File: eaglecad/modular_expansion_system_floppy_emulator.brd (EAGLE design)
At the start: 90.5 x 100 mm, 35 parts, among them IC1 74LS00N, IC11 74LS20N, IC2 74LS373N, IC3 74LS30N, IC4 74LS244N, IC5 74S74N, IC6 74LS139N, IC7 74LS155N, J1_ADDRESS_CON J1, J1_TEENSY_CON TEENSY_CON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

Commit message: all three boards designed
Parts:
- removed J3_WAIT_AND_INTERRUPT_BLOCK: J3, SparkFun-Connectors:1X20
- added J1-WAIT-AND-INT: WAIT-AND-INT, SparkFun-Connectors:2X4
- moved IC6 20.0 mm to (83.5, 81.0), turned to 270 degrees
- moved H5 0.08 mm to (85.1, 5.08)
- moved H6 0.07 mm to (14.6, 5.08)
- moved H2 0.07 mm to (14.6, 95.2)
- moved H4 0.06 mm to (85.1, 95.2)
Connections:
- removed net INT1*: J3_WAIT_AND_INTERRUPT_BLOCK.2
- removed net INT2*: J3_WAIT_AND_INTERRUPT_BLOCK.3
- removed net INT3*: J3_WAIT_AND_INTERRUPT_BLOCK.4
- removed net INT4*: J3_WAIT_AND_INTERRUPT_BLOCK.5
- removed net INT5*: J3_WAIT_AND_INTERRUPT_BLOCK.6
- removed net INT6*: J3_WAIT_AND_INTERRUPT_BLOCK.7
- removed net INT7*: J3_WAIT_AND_INTERRUPT_BLOCK.8
- removed net WAIT1*: J3_WAIT_AND_INTERRUPT_BLOCK.14
- removed net WAIT2*: J3_WAIT_AND_INTERRUPT_BLOCK.15
- removed net WAIT3*: J3_WAIT_AND_INTERRUPT_BLOCK.16
- removed net WAIT4*: J3_WAIT_AND_INTERRUPT_BLOCK.17
- removed net WAIT5*: J3_WAIT_AND_INTERRUPT_BLOCK.18
- removed net WAIT6*: J3_WAIT_AND_INTERRUPT_BLOCK.19
- removed net WAIT7*: J3_WAIT_AND_INTERRUPT_BLOCK.20
- net INT0*: now also J1-WAIT-AND-INT.1; no longer J3_WAIT_AND_INTERRUPT_BLOCK.1
- net WAIT0*: now also J1-WAIT-AND-INT.2; no longer J3_WAIT_AND_INTERRUPT_BLOCK.13
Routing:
- net INT0*: track 75.1 -> 154.3 mm
- net A11: track 19.4 -> 59.9 mm, vias 1 -> 0
- net XX11X111111XXXX: track 14.2 -> 48.5 mm, vias 0 -> 1
- net 37EX_: track 48.8 -> 80.1 mm, vias 1 -> 0
- net A14: track 15.4 -> 45.8 mm
- net A15: track 15.7 -> 43.9 mm, vias 0 -> 2
- net WAIT0*: track 9.63 -> 30.9 mm, vias 0 -> 1
- net RAS*: track 134.8 -> 119.3 mm
- net 3XXX_: track 9.76 -> 19.2 mm
- net WR*: track 63.5 -> 70.6 mm, vias 2 -> 4
- net RD*: track 28.9 -> 25.2 mm, vias 0 -> 2

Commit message: added text to boards
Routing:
- net D3: track 140.6 -> 144.5 mm
- net D5_HV: track 65.7 -> 68.2 mm
- net P18: track 51.5 -> 52.7 mm
- net 37E4RD_: track 72.2 -> 73.3 mm
- net 37E8WR_: track 35.3 -> 36.2 mm
- net D0_LV: track 48.9 -> 48.0 mm
- net A1_LV: track 66.2 -> 66.9 mm
- net VCC/2: track 151.5 -> 152.2 mm
- net D2_LV: track 51.0 -> 50.4 mm
- net 37E0WR_LV_: track 47.2 -> 46.6 mm
- net 37E4WR_LV_: track 26.6 -> 27.2 mm
- net P17: track 56.3 -> 56.8 mm
- net INTERUPT_TO_TRS80_LV_: track 37.6 -> 38.2 mm
- net A0: track 126.4 -> 125.9 mm
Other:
- board text added: "TRS80MXS Floppy V1.0 Joe Rounceville (C)2019"

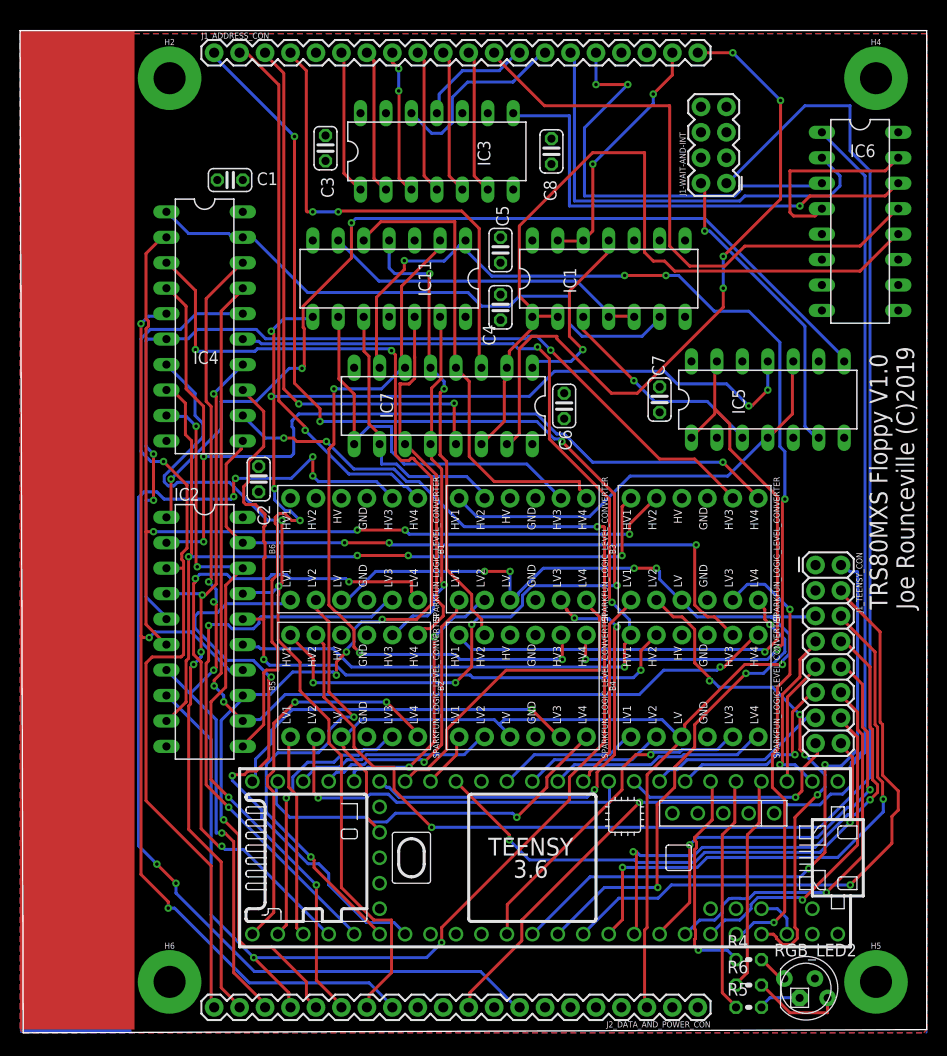
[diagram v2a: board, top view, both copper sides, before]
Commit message: removed soft reset for vdp, added 12 voice sound
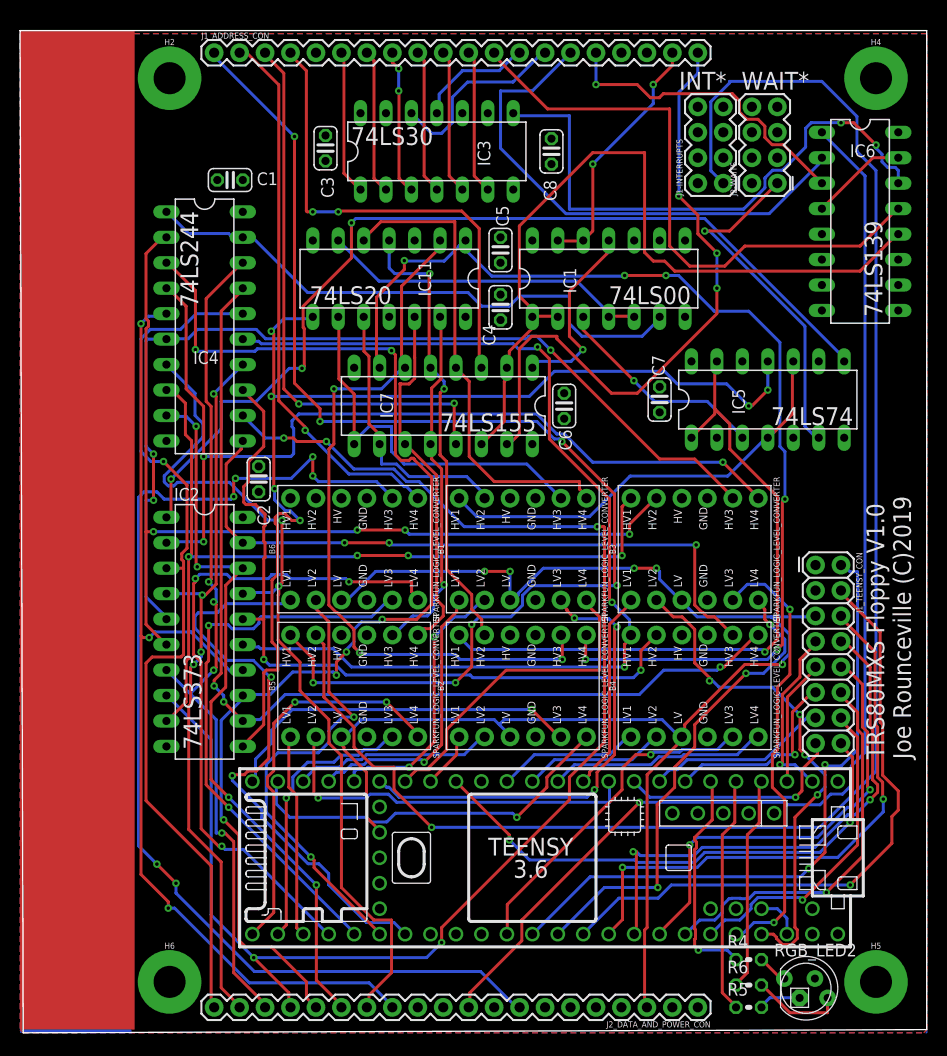
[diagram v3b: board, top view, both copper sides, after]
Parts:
- removed J1-WAIT-AND-INT: WAIT-AND-INT, SparkFun-Connectors:2X4
- added J1-INTERRUPTS: INTERRUPTS, SparkFun-Connectors:2X4
- added J2-WAITS: WAITS, SparkFun-Connectors:2X4
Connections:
- net INT0*: now also J1-INTERRUPTS.1; no longer J1-WAIT-AND-INT.1
- net WAIT0*: now also J2-WAITS.1; no longer J1-WAIT-AND-INT.2
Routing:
- net A15: track 43.9 -> 31.4 mm, vias 2 -> 1
- net 3XXX_: track 19.2 -> 9.72 mm
- net INT0*: track 154.3 -> 163.5 mm
- net XX11X111111XXXX: track 48.5 -> 57.0 mm, vias 1 -> 2
- net WR*: track 70.6 -> 64.6 mm, vias 4 -> 3
- net A14: track 45.8 -> 51.6 mm
- net WAIT0*: track 30.9 -> 35.0 mm
- net RAS*: track 119.3 -> 117.1 mm
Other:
- board text added: "74LS00"
- board text added: "74LS139"
- board text added: "74LS155"
- board text added: "74LS20"
- board text added: "74LS244"
- board text added: "74LS30"
- board text added: "74LS373"
- board text added: "74LS74"
- board text added: "INT*"
- board text added: "WAIT*"

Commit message: boards as they were when sent to allpcb
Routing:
- net D0_LV: track 48.0 -> 51.0 mm
- net VCC/2: track 152.2 -> 153.5 mm
- net D4: track 119.9 -> 120.9 mm
- net D6: track 87.9 -> 87.2 mm
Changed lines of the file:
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@@
 <wire x1="32.25" y1="38.25" x2="33" y2="39" width="0.3" layer="16"/>
 <wire x1="32.25" y1="38" x2="32.25" y2="38.25" width="0.3" layer="16"/>
-<wire x1="31.25" y1="37" x2="32.25" y2="38" width="0.3" layer="1"/>
-<wire x1="31.25" y1="35.6825" x2="31.25" y2="37" width="0.3" layer="1"/>
 <wire x1="30.9325" y1="36" x2="31.25" y2="35.6825" width="0.3" layer="16"/>
 <wire x1="30.9325" y1="36" x2="26.885" y2="36" width="0.3" layer="16"/>
@@
 <wire x1="28.2575" y1="5.08" x2="28.2575" y2="3.4925" width="0.3" layer="1"/>
 <wire x1="28.2575" y1="3.4925" x2="29.21" y2="2.54" width="0.3" layer="1"/>
+<wire x1="31.115" y1="38.1" x2="32.15" y2="38.1" width="0.3" layer="1"/>
+<wire x1="32.15" y1="38.1" x2="32.25" y2="38" width="0.3" layer="1"/>
+<wire x1="31.25" y1="35.6825" x2="30.9524" y2="35.9801" width="0.3" layer="1"/>
+<wire x1="30.9524" y1="37.9374" x2="31.115" y2="38.1" width="0.3" layer="1"/>
+<wire x1="30.9524" y1="35.9801" x2="30.9524" y2="37.9374" width="0.3" layer="1"/>
 </signal>
 <signal name="D6">
@@
 <wire x1="30.5" y1="28.905" x2="30.5" y2="31.25" width="0.3" layer="1"/>
 <wire x1="31.75" y1="27.655" x2="30.5" y2="28.905" width="0.3" layer="1"/>
-<wire x1="31.75" y1="14.5" x2="31.75" y2="27.655" width="0.3" layer="1"/>
-<wire x1="35" y1="11.25" x2="31.75" y2="14.5" width="0.3" layer="1"/>
-<wire x1="36.75" y1="11.25" x2="35" y2="11.25" width="0.3" layer="1"/>
-<wire x1="36.75" y1="6" x2="36.75" y2="11.25" width="0.3" layer="1"/>
+<wire x1="31.75" y1="27.655" x2="31.75" y2="17.8375" width="0.3" layer="1"/>
+<wire x1="36.75" y1="12.8375" x2="36.75" y2="6" width="0.3" layer="1"/>
 <wire x1="34.5" y1="3.75" x2="36.75" y2="6" width="0.3" layer="1"/>
 <wire x1="34.5" y1="2.75" x2="34.5" y2="3.75" width="0.3" layer="1"/>
@@
 <wire x1="14.0694" y1="55.5694" x2="17.9306" y2="59.4306" width="0.3" layer="16"/>
 <wire x1="24.3375" y1="51.1625" x2="20.5725" y2="54.9275" width="0.3" layer="16"/>
+<wire x1="31.75" y1="17.8375" x2="34.521" y2="15.0665" width="0.3" layer="1"/>
+<wire x1="34.521" y1="15.0665" x2="34.521" y2="14.49213125" width="0.3" layer="1"/>
+<wire x1="34.521" y1="14.49213125" x2="35.12963125" y2="13.8835" width="0.3" layer="1"/>
+<wire x1="35.12963125" y1="13.8835" x2="35.704" y2="13.8835" width="0.3" layer="1"/>
+<wire x1="35.704" y1="13.8835" x2="36.75" y2="12.8375" width="0.3" layer="1"/>
 </signal>
 <signal name="D7">
@@
 <contactref element="J1_TEENSY_CON" pad="5"/>
 <wire x1="67.25" y1="41.5" x2="65.75" y2="43" width="0.3" layer="16"/>
-<wire x1="79" y1="41.5" x2="74.6125" y2="41.5" width="0.3" layer="16"/>
-<wire x1="74.6125" y1="41.5" x2="67.25" y2="41.5" width="0.3" layer="16"/>
+<wire x1="79" y1="41.5" x2="74.71251875" y2="41.5" width="0.3" layer="16"/>
+<wire x1="74.71251875" y1="41.5" x2="67.25" y2="41.5" width="0.3" layer="16"/>
 <wire x1="65.75" y1="43" x2="65.7225" y2="43.18" width="0.3" layer="16"/>
 <wire x1="79" y1="41.5" x2="79.0575" y2="41.5925" width="0.3" layer="16"/>
 <wire x1="31.75" y1="43.18" x2="32.315" y2="43.18" width="0.3" layer="16"/>
-<wire x1="65.7225" y1="43.18" x2="65.5" y2="43.25" width="0.3" layer="16"/>
 <wire x1="34.25" y1="21.5" x2="35.5" y2="20.25" width="0.3" layer="1"/>
 <wire x1="34.25" y1="26" x2="34.25" y2="21.5" width="0.3" layer="1"/>
@@
 <wire x1="51.89596875" y1="46.355" x2="49.3673" y2="43.82633125" width="0.3" layer="16"/>
 <via x="60.96" y="46.355" extent="1-16" drill="0.35"/>
-<wire x1="63.5" y1="46.0375" x2="63.1825" y2="46.355" width="0.3" layer="16"/>
-<wire x1="63.5" y1="46.0375" x2="63.5" y2="45.25" width="0.3" layer="16"/>
-<wire x1="65.5" y1="43.25" x2="63.5" y2="45.25" width="0.3" layer="16"/>
-<via x="63.1825" y="46.355" extent="1-16" drill="0.35"/>
-<wire x1="60.96" y1="46.355" x2="63.1825" y2="46.355" width="0.3" layer="1"/>
+<wire x1="65.7225" y1="43.18" x2="65.7225" y2="46.355" width="0.3" layer="16"/>
+<via x="65.7225" y="46.355" extent="1-16" drill="0.35"/>
+<wire x1="60.96" y1="46.355" x2="65.7225" y2="46.355" width="0.3" layer="1"/>
 <wire x1="48.5775" y1="43.18" x2="48.9125" y2="43.18" width="0.3" layer="16"/>
 <wire x1="48.9125" y1="43.18" x2="49.3673" y2="43.6348" width="0.3" layer="16"/>
@@
 <wire x1="66" y1="30.75" x2="72" y2="36.75" width="0.3" layer="1"/>
 <wire x1="75.75" y1="36.75" x2="75.75" y2="37.11020625" width="0.3" layer="16"/>
-<wire x1="74.78191875" y1="41.4306" x2="74.6819" y2="41.4306" width="0.3" layer="16"/>
-<wire x1="74.6819" y1="41.4306" x2="74.6125" y2="41.5" width="0.3" layer="16"/>
 <wire x1="75.75" y1="37.11020625" x2="76.4524" y2="37.81260625" width="0.3" layer="16"/>
 <wire x1="76.4524" y1="37.81260625" x2="76.4524" y2="39.76011875" width="0.3" layer="16"/>
-<wire x1="76.4524" y1="39.76011875" x2="74.78191875" y2="41.4306" width="0.3" layer="16"/>
+<wire x1="76.4524" y1="39.76011875" x2="74.71251875" y2="41.5" width="0.3" layer="16"/>
 </signal>
 <signal name="FLIPFLOP_PRE_LV">
@@
 <wire x1="67" y1="30.75" x2="67" y2="28.5" width="0.3" layer="1"/>
 <wire x1="72.115" y1="35.865" x2="67" y2="30.75" width="0.3" layer="1"/>
-<wire x1="75.99125" y1="37.99125" x2="73.865" y2="35.865" width="0.3" layer="16"/>
+<wire x1="73.865" y1="35.865" x2="75.99125" y2="37.99125" width="0.3" layer="16"/>
 <wire x1="73.865" y1="35.865" x2="72.115" y2="35.865" width="0.3" layer="16"/>
-<wire x1="74" y1="41.25" x2="74.5" y2="40.75" width="0.3" layer="1"/>
-<wire x1="74" y1="42.25" x2="74" y2="41.25" width="0.3" layer="1"/>
-<wire x1="73.5" y1="42.75" x2="74" y2="42.25" width="0.3" layer="1"/>
-<wire x1="73.5" y1="43" x2="73.5" y2="42.75" width="0.3" layer="1"/>
 <wire x1="53.5" y1="10" x2="53.34" y2="9.8425" width="0.3" layer="16"/>
-<wire x1="73.5" y1="43" x2="73.3425" y2="43.18" width="0.3" layer="1"/>
 <via x="63.3175" y="14.5" extent="1-16" drill="0.35"/>
 <via x="72.115" y="35.865" extent="1-16" drill="0.35"/>
-<via x="74.5" y="40.75" extent="1-16" drill="0.35"/>
-<wire x1="75.99125" y1="37.99125" x2="75.99125" y2="39.25875" width="0.3" layer="16"/>
-<wire x1="75.99125" y1="39.25875" x2="74.5" y2="40.75" width="0.3" layer="16"/>
+<via x="71.96" y="40.75" extent="1-16" drill="0.35"/>
+<wire x1="73.3425" y1="43.18" x2="73.3425" y2="42.1325" width="0.3" layer="1"/>
+<wire x1="73.3425" y1="42.1325" x2="71.96" y2="40.75" width="0.3" layer="1"/>
+<wire x1="75.99125" y1="39.57875" x2="74.6125" y2="40.9575" width="0.3" layer="16"/>
+<wire x1="72.1675" y1="40.9575" x2="71.96" y2="40.75" width="0.3" layer="16"/>
+<wire x1="75.99125" y1="37.99125" x2="75.99125" y2="39.57875" width="0.3" layer="16"/>
+<wire x1="74.6125" y1="40.9575" x2="72.1675" y2="40.9575" width="0.3" layer="16"/>
 </signal>
 <signal name="D1_LV">

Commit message: updated sound board, fixed mirrored headers
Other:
- board text added: "3.3v"
- board text added: "5v"
- board text added: "a0"
- board text added: "a1"
- board text added: "d0"
- board text added: "d1"
- board text added: "d2"
- board text added: "d3"
- board text added: "d4"
- board text added: "d5"
- board text added: "d6"
- board text added: "d7"
- board text added: "gnd"
- board text added: "wr*"
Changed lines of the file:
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@@
 <text x="70.1675" y="95.885" size="1.778" layer="25" rot="R180">INT*</text>
 <text x="78.4225" y="95.885" size="1.778" layer="25" rot="R180">WAIT*</text>
+<text x="17.78" y="93.98" size="1.778" layer="25">a0</text>
+<text x="20.32" y="92.3925" size="1.778" layer="25">a1</text>
+<text x="68.8975" y="97.155" size="1.778" layer="25">wr*</text>
+<text x="17.78" y="4.1275" size="1.778" layer="25">d0</text>
+<text x="20.32" y="5.715" size="1.778" layer="25">d1</text>
+<text x="22.86" y="4.1275" size="1.778" layer="25">d2</text>
+<text x="25.4" y="5.715" size="1.778" layer="25">d3</text>
+<text x="27.6225" y="3.81" size="1.778" layer="25">d4</text>
+<text x="30.1625" y="5.715" size="1.778" layer="25">d5</text>
+<text x="33.02" y="3.81" size="1.778" layer="25">d6</text>
+<text x="35.2425" y="5.715" size="1.778" layer="25">d7</text>
+<text x="66.04" y="3.81" size="1.778" layer="25">5v</text>
+<text x="62.865" y="5.3975" size="1.778" layer="25">gnd</text>
+<text x="59.69" y="3.81" size="1.778" layer="25">3.3v</text>
 </plain>
 <attributes>

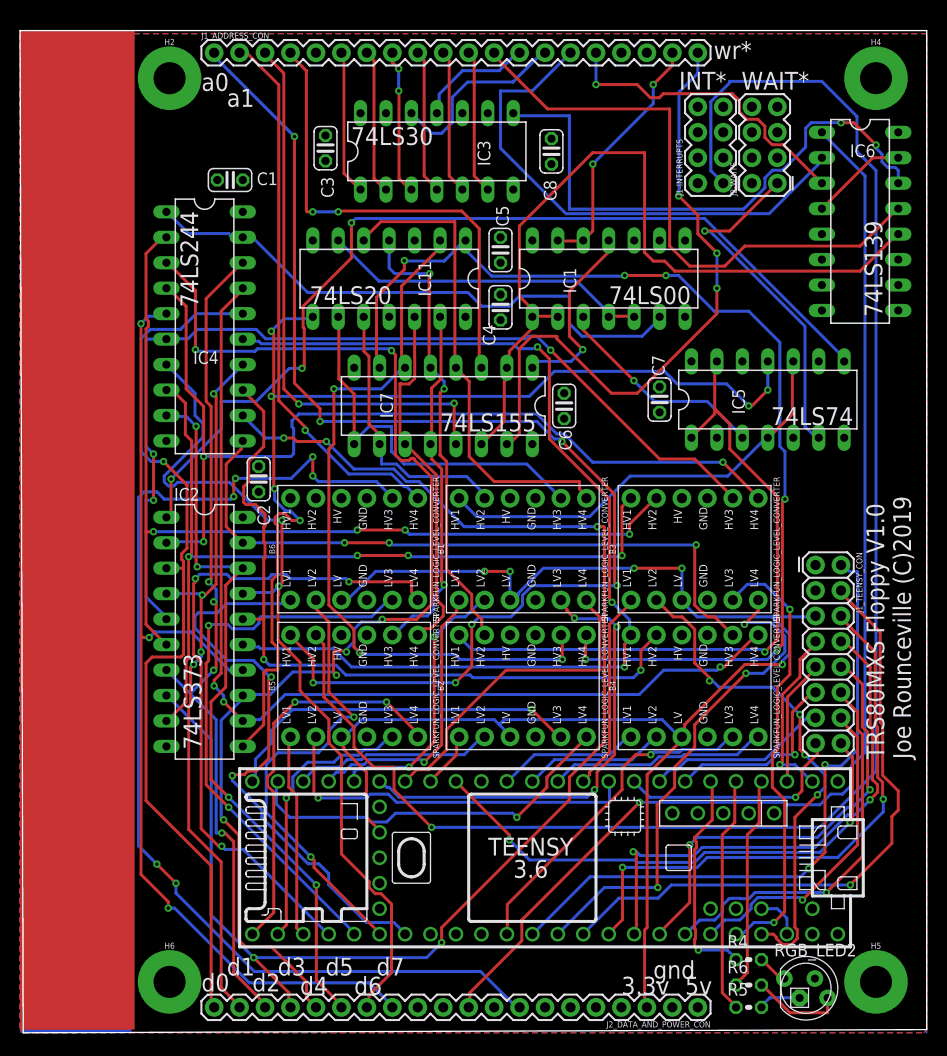
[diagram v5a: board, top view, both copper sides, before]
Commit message: implemented pacman fruit behavior
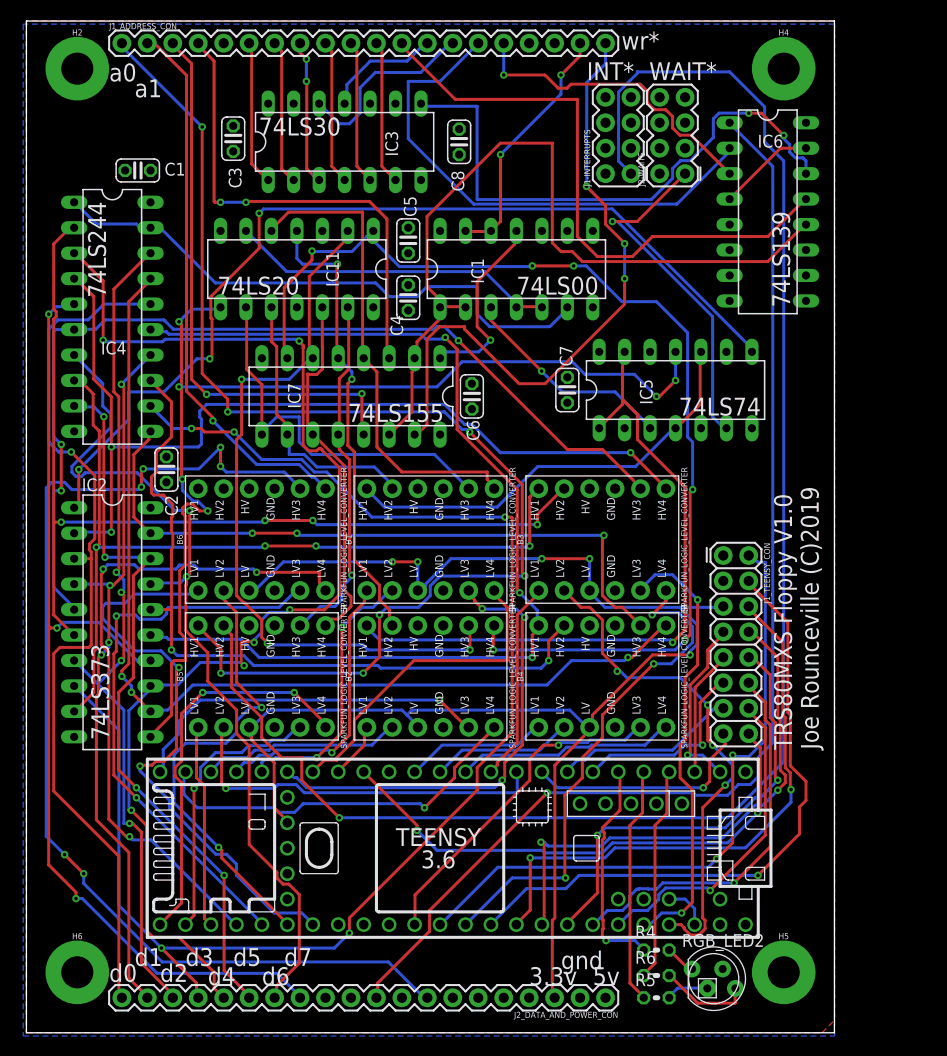
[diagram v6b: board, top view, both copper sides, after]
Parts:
- moved B3 9.26 mm to (57.8, 49.2)
- moved B4 9.26 mm to (57.8, 35.6)
- moved H4 9.26 mm to (75.9, 96.2)
- moved H5 9.26 mm to (75.9, 6.03)
- moved J1_TEENSY_CON 9.26 mm to (69.8, 47.6)
- moved J2-WAITS 9.26 mm to (64.8, 89.5)
- moved RGB_LED2 9.26 mm to (68.9, 5.40)
- moved C7 9.26 mm to (54.3, 64.1)
- moved B5 9.26 mm to (23.8, 35.6)
- moved B6 9.26 mm to (23.8, 49.2)
- moved C3 9.26 mm to (21.0, 89.2)
- moved C4 9.26 mm to (38.4, 73.3)
- moved C5 9.26 mm to (38.4, 79.1)
- moved C6 9.26 mm to (44.8, 63.5)
- moved IC1 9.26 mm to (49.2, 76.2)
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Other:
- board size 90.5 x 100 mm -> 80.6 x 101 mm
